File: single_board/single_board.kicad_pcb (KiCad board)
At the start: 4 copper layers, 118.6 x 108.9 mm, 120 parts, among them J1 SWD, J11 SPI Debug, J17 BOOTSEL, J2 USB_C_Receptacle_USB2.0_16P, J3 RST, J30 JST_GH_H, J31 JST_GH_H, J32 PB_Vertical, J33 JST_GH_H, J34 PB_Vertical, J35 JST_GH_H, J36 JST_GH_H, J37 JST_GH_H, J38 PB_Vertical, J39 PB_Vertical, J4 Conn_01x02, J40 PB_Vertical, J41 PB_Vertical, J42 PB_Vertical, J43 PB_Vertical, J44 PB_Vertical, J45 PB_Vertical, J46 PB_Vertical, J47 PB_Vertical, J48 PB_Vertical, J49 PB_Vertical, J5 Conn_01x02, J51 JST_GH_H, J6 Conn_01x02, Q1 AO3401A, Q2 AO3401A, Q3 AO3401A, Q4 AO3401A, Q5 2N7002, SW1 Button, U1 AP2112K-3.3, U3 USBLC6-2SC6, U4 LSM6DSV, U5 STM32G474VBTx, Y1 FC-135

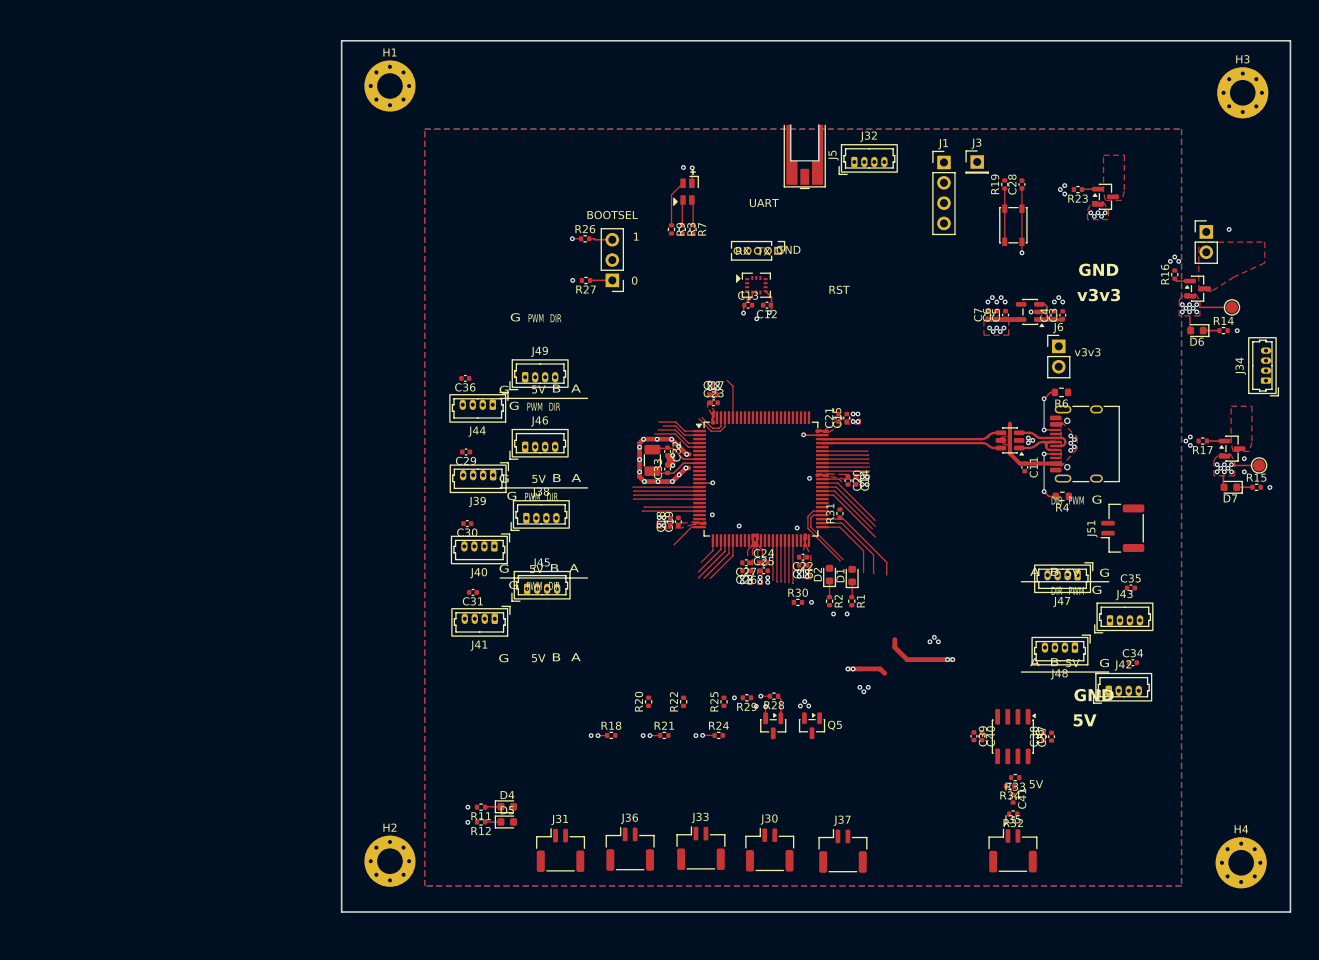
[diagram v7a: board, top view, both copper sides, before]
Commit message: M8 mounting holes
better picoblade arrangement
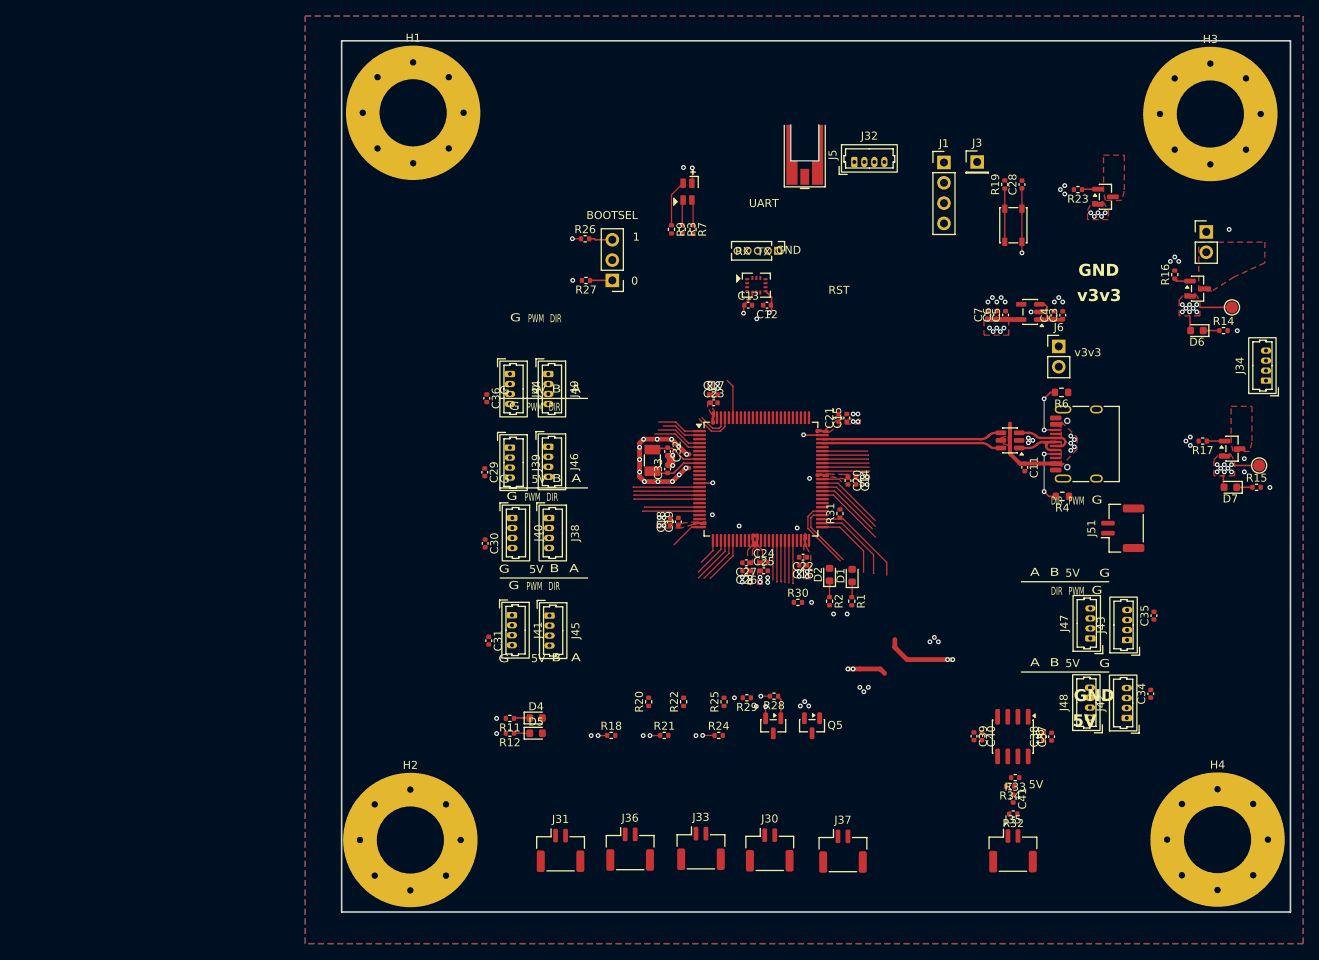
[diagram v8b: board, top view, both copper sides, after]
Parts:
- H1, H2, H3, H4: footprint MountingHole:MountingHole_3.2mm_M3_Pad_Via -> MountingHole:MountingHole_8.4mm_M8_Pad_Via
- moved R11 11.7 mm to (118.6, 143.9)
- moved R12 11.7 mm to (118.6, 145.8)
- moved D4 11.7 mm to (121.9, 143.9)
- moved D5 11.7 mm to (121.9, 145.8)
- moved J48 8.95 mm to (191.2, 143.8), turned to 90 degrees
- moved J47 8.06 mm to (191.2, 133.9), turned to 90 degrees
- moved C31 6.34 mm to (116.0, 134.2), turned to -90 degrees
- moved H3 4.84 mm to (206.2, 68.4)
- moved C35 4.49 mm to (199.2, 131.1), turned to 90 degrees
- moved C34 4.47 mm to (198.8, 140.9), turned to 90 degrees
- moved H1 4.43 mm to (106.5, 68.2)
- moved J44 4.41 mm to (118.7, 100.9), turned to -90 degrees
- moved J45 4.37 mm to (123.6, 131.1), turned to -90 degrees
- moved J40 4.20 mm to (119.0, 118.9), turned to -90 degrees
- moved H4 4.14 mm to (207.1, 159.1)
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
